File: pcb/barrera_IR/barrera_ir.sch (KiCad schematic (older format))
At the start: 16 parts, among them J1 RJ45, P1 DIN_5, P2 DIN_5, U1 LM358N

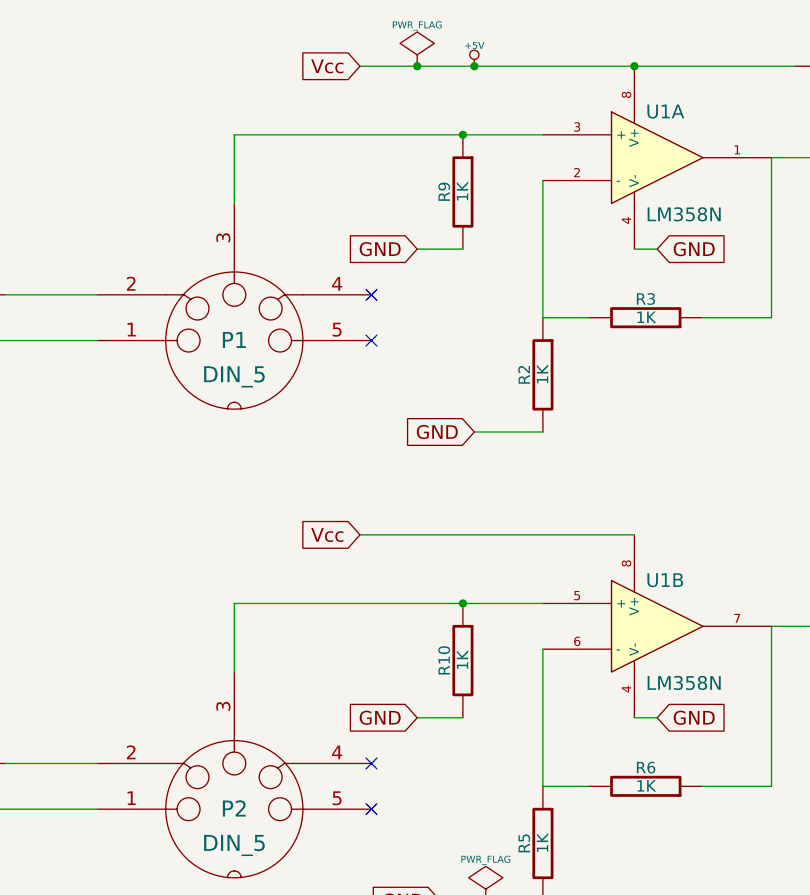
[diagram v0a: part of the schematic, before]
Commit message: correction bug in circuit of infra red barrier
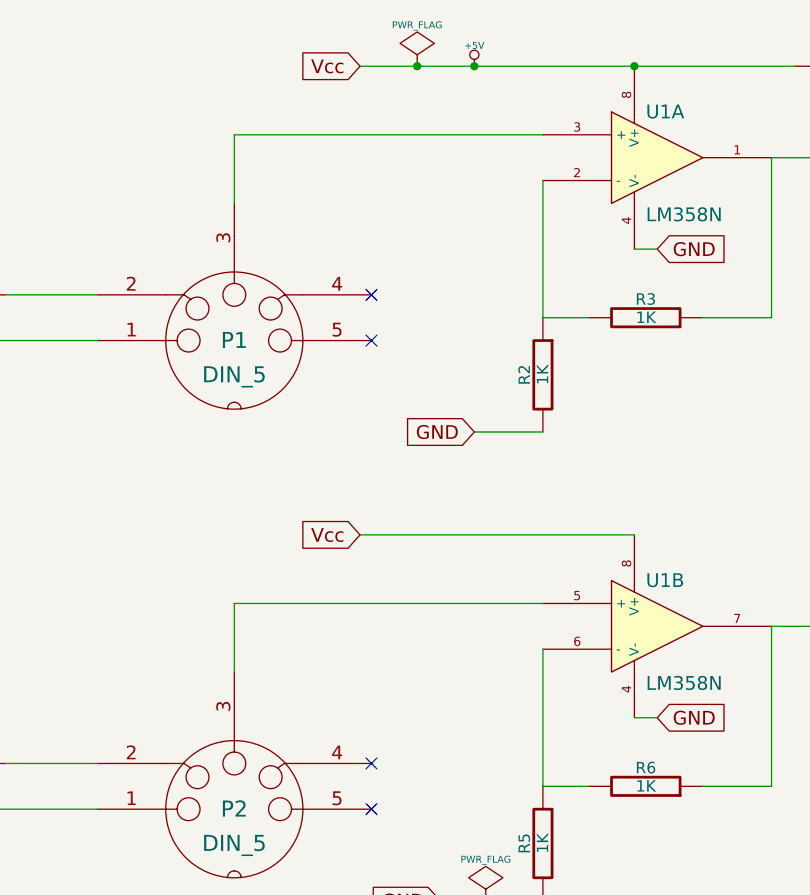
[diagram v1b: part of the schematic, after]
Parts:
- removed R10, R9: 1K, symbol R
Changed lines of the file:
@@
-EESchema Schematic File Version 2  date mar 21 may 2013 21:48:05 UYT
+EESchema Schematic File Version 2  date mié 22 may 2013 19:52:20 UYT
 LIBS:power
 LIBS:device
@@
 LIBS:valves
 LIBS:barrera_ir-cache
-EELAYER 24 0
+EELAYER 27 0
 EELAYER END
 $Descr A4 11693 8268
@@
 F 0 "P1" H 4350 3850 70  0000 C CNN
 F 1 "DIN_5" H 4350 3700 70  0000 C CNN
-F 2 "" H 4350 3850 60  0001 C CNN
-F 3 "" H 4350 3850 60  0001 C CNN
 	1    4350 3850
 	1    0    0    -1
@@
 F 0 "#PWR01" H 5400 2740 20  0001 C CNN
 F 1 "+5V" H 5400 2740 30  0000 C CNN
-F 2 "" H 5400 2650 60  0001 C CNN
-F 3 "" H 5400 2650 60  0001 C CNN
 	1    5400 2650
 	1    0    0    -1
@@
 F 0 "#FLG02" H 5150 2745 30  0001 C CNN
 F 1 "PWR_FLAG" H 5150 2830 30  0000 C CNN
-F 2 "" H 5150 2650 60  0001 C CNN
-F 3 "" H 5150 2650 60  0001 C CNN
 	1    5150 2650
 	1    0    0    -1
@@
 F 0 "R1" V 3180 3650 50  0000 C CNN
 F 1 "390" V 3100 3650 50  0000 C CNN
-F 2 "" H 3100 3650 60  0001 C CNN
-F 3 "" H 3100 3650 60  0001 C CNN
 	1    3100 3650
 	0    1    1    0
@@
 F 0 "R3" V 6230 3750 50  0000 C CNN
 F 1 "1K" V 6150 3750 50  0000 C CNN
-F 2 "" H 6150 3750 60  0001 C CNN
-F 3 "" H 6150 3750 60  0001 C CNN
 	1    6150 3750
 	0    1    -1   0
@@
 F 0 "D1" H 7450 3150 40  0000 C CNN
 F 1 "1N4148" H 7450 2950 40  0000 C CNN
-F 2 "" H 7450 3050 60  0001 C CNN
-F 3 "" H 7450 3050 60  0001 C CNN
 	1    7450 3050
 	-1   0    0    1
@@
 F 0 "U1" H 6150 3250 60  0000 L CNN
 F 1 "LM358N" H 6150 2800 60  0000 L CNN
-F 2 "" H 6200 3050 60  0000 C CNN
-F 3 "" H 6200 3050 60  0000 C CNN
 	1    6200 3050
 	1    0    0    -1
@@
 F 0 "R2" V 5780 4000 50  0000 C CNN
 F 1 "1K" V 5700 4000 50  0000 C CNN
-F 2 "" H 5700 4000 60  0001 C CNN
-F 3 "" H 5700 4000 60  0001 C CNN
 	1    5700 4000
 	-1   0    0    -1
@@
 F 0 "P2" H 4350 5900 70  0000 C CNN
 F 1 "DIN_5" H 4350 5750 70  0000 C CNN
-F 2 "" H 4350 5900 60  0001 C CNN
-F 3 "" H 4350 5900 60  0001 C CNN
 	1    4350 5900
 	1    0    0    -1
@@
 F 0 "R4" V 3180 5700 50  0000 C CNN
 F 1 "390" V 3100 5700 50  0000 C CNN
-F 2 "" H 3100 5700 60  0001 C CNN
-F 3 "" H 3100 5700 60  0001 C CNN
 	1    3100 5700
 	0    1    1    0
@@
 F 0 "R6" V 6230 5800 50  0000 C CNN
 F 1 "1K" V 6150 5800 50  0000 C CNN
-F 2 "" H 6150 5800 60  0001 C CNN
-F 3 "" H 6150 5800 60  0001 C CNN
 	1    6150 5800
 	0    1    -1   0
@@
 F 0 "D2" H 7450 5200 40  0000 C CNN
 F 1 "1N4148" H 7450 5000 40  0000 C CNN
-F 2 "" H 7450 5100 60  0001 C CNN
-F 3 "" H 7450 5100 60  0001 C CNN
 	1    7450 5100
 	-1   0    0    1
@@
 F 0 "U1" H 6150 5300 60  0000 L CNN
 F 1 "LM358N" H 6150 4850 60  0000 L CNN
-F 2 "" H 6200 5100 60  0000 C CNN
-F 3 "" H 6200 5100 60  0000 C CNN
 	2    6200 5100
 	1    0    0    -1
@@
 F 0 "R5" V 5780 6050 50  0000 C CNN
 F 1 "1K" V 5700 6050 50  0000 C CNN
-F 2 "" H 5700 6050 60  0001 C CNN
-F 3 "" H 5700 6050 60  0001 C CNN
 	1    5700 6050
 	-1   0    0    -1
@@
 F 0 "R7" V 7130 2650 50  0000 C CNN
 F 1 "1K" V 7050 2650 50  0000 C CNN
-F 2 "" H 7050 2650 60  0001 C CNN
-F 3 "" H 7050 2650 60  0001 C CNN
 	1    7050 2650
 	0    1    -1   0
@@
 F 0 "#PWR03" H 5450 6400 30  0001 C CNN
 F 1 "GND" H 5450 6330 30  0001 C CNN
-F 2 "" H 5450 6400 60  0000 C CNN
-F 3 "" H 5450 6400 60  0000 C CNN
 	1    5450 6400
 	1    0    0    -1
@@
 F 0 "#FLG04" H 5450 6395 30  0001 C CNN
 F 1 "PWR_FLAG" H 5450 6480 30  0000 C CNN
-F 2 "" H 5450 6300 60  0000 C CNN
-F 3 "" H 5450 6300 60  0000 C CNN
 	1    5450 6300
 	1    0    0    -1
@@
 F 0 "R8" V 9380 5700 50  0000 C CNN
 F 1 "4K7" V 9300 5700 50  0000 C CNN
-F 2 "" H 9300 5700 60  0001 C CNN
-F 3 "" H 9300 5700 60  0001 C CNN
 	1    9300 5700
 	0    1    -1   0
@@
 Wire Wire Line
 	9750 5700 9550 5700
-$Comp
-L R R10
-U 1 1 519BF9E2
-P 5350 5250
-F 0 "R10" V 5430 5250 50  0000 C CNN
-F 1 "1K" V 5350 5250 50  0000 C CNN
-F 2 "" H 5350 5250 60  0001 C CNN
-F 3 "" H 5350 5250 60  0001 C CNN
-	1    5350 5250
-	-1   0    0    -1
-$EndComp
-Text GLabel 5150 5500 0    60   Input ~ 0
-GND
 Wire Wire Line
 	4350 5300 4350 5000
 Wire Wire Line
 	4350 5000 5700 5000
-Connection ~ 5350 5000
-Wire Wire Line
-	5350 5500 5150 5500
-$Comp
-L R R9
-U 1 1 519BFB8A
-P 5350 3200
-F 0 "R9" V 5430 3200 50  0000 C CNN
-F 1 "1K" V 5350 3200 50  0000 C CNN
-F 2 "" H 5350 3200 60  0001 C CNN
-F 3 "" H 5350 3200 60  0001 C CNN
-	1    5350 3200
-	-1   0    0    -1
-$EndComp
-Text GLabel 5150 3450 0    60   Input ~ 0
-GND
 Wire Wire Line
 	4350 2950 5700 2950
-Connection ~ 5350 2950
-Wire Wire Line
-	5350 3450 5150 3450
 Wire Wire Line
 	4350 2950 4350 3250

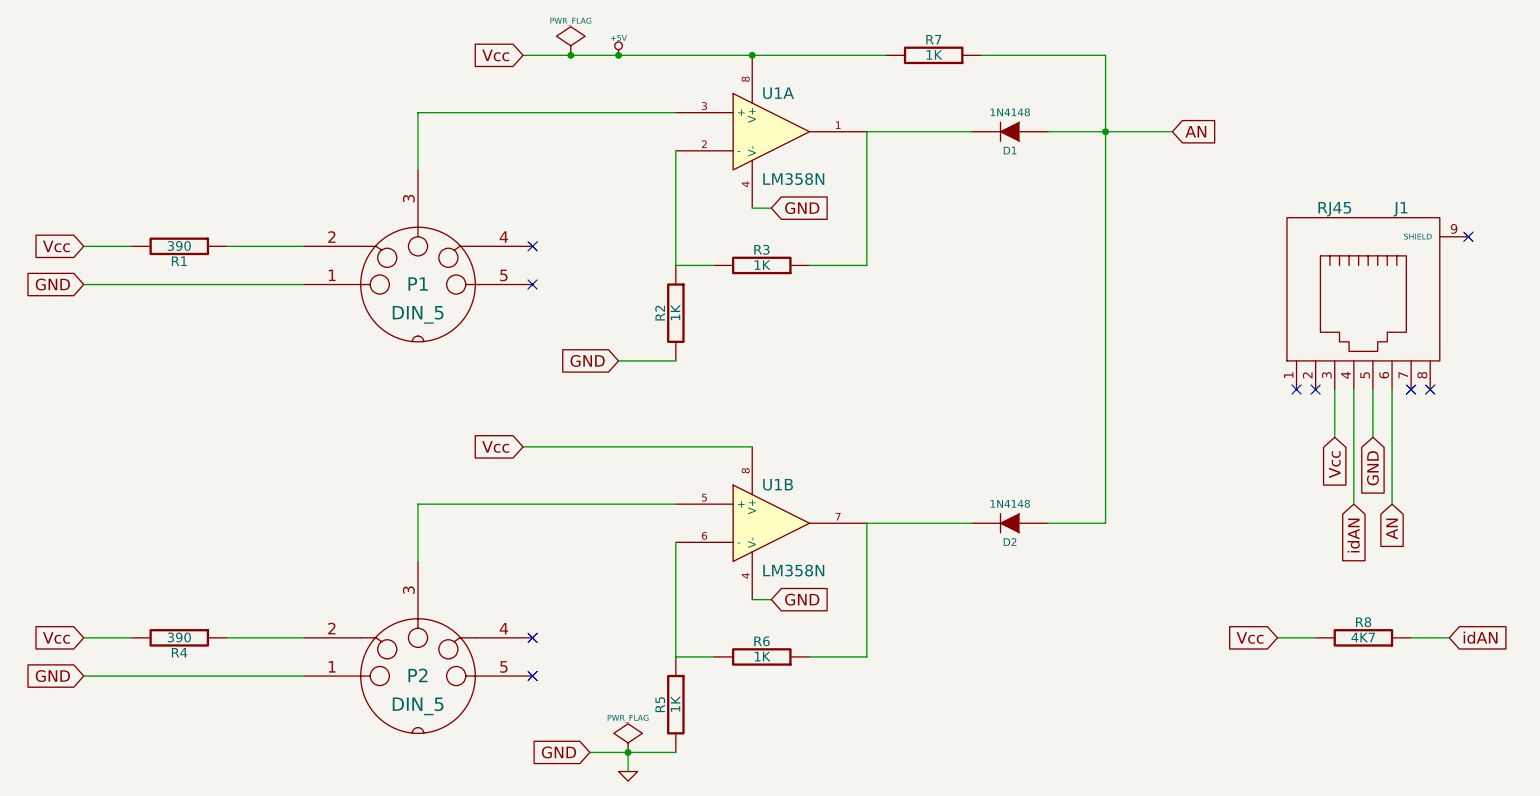
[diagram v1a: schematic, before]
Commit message: Change the wired AND for wired OR in the output of barrier IR
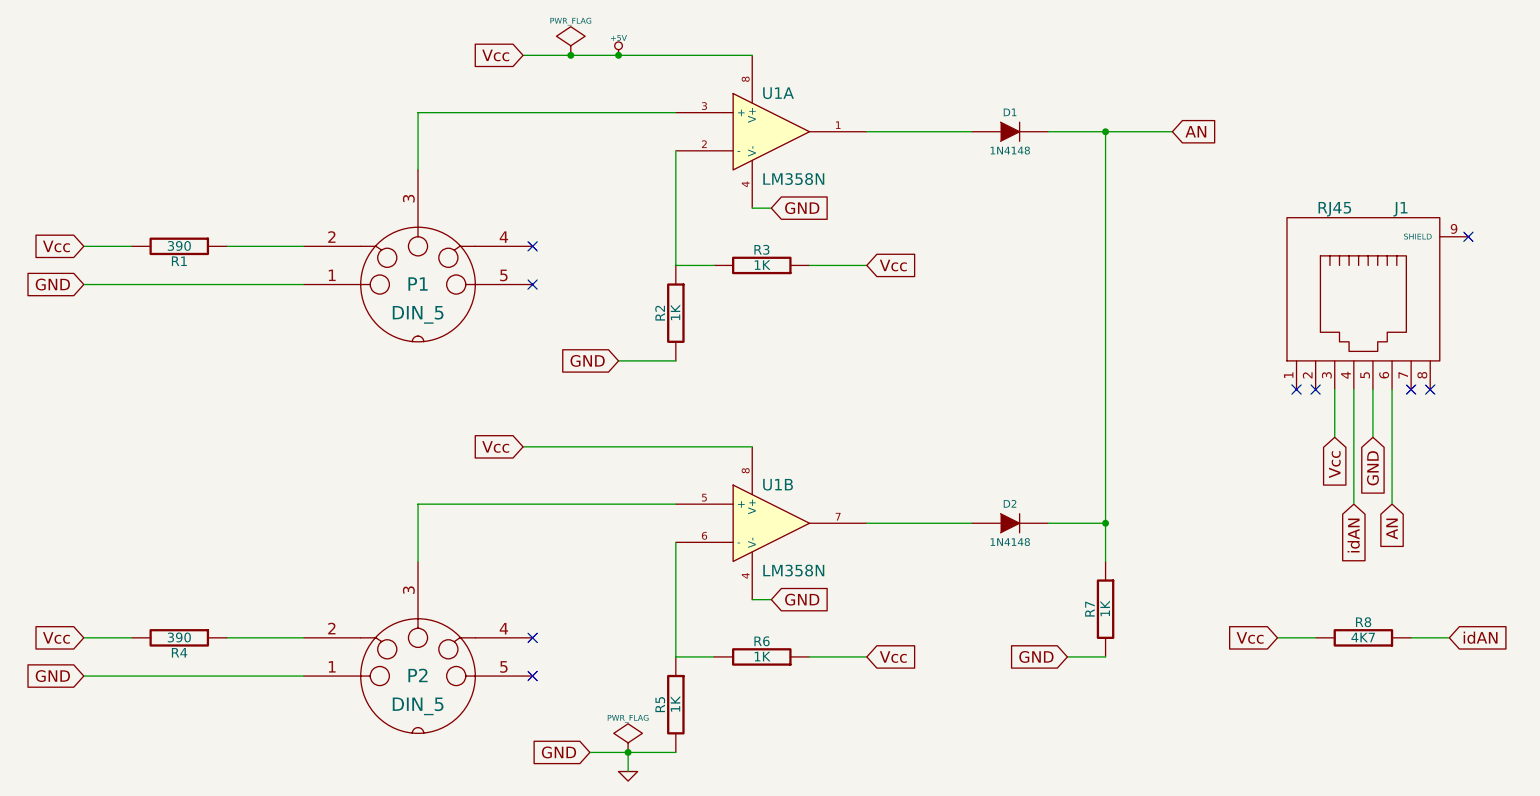
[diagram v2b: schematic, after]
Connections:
- net +5V: now also R3.1, R6.1; no longer R7.2
- net AN: now also D1.2 (K), D2.2 (K); no longer D1.1 (A), D2.1 (A)
- net GND: now also R7.2
- new net: D1.1 (A), U1.1
- new net: D2.1 (A), U1.7
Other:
- moved on the sheet: R7
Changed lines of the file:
@@
-EESchema Schematic File Version 2  date mié 22 may 2013 19:52:20 UYT
+EESchema Schematic File Version 2  date mar 25 jun 2013 20:22:33 UYT
 LIBS:power
 LIBS:device
@@
 Sheet 1 1
 Title "Barrera infrarojo para detectar movimiento"
-Date "22 may 2013"
-Rev "1"
+Date "25 jun 2013"
+Rev "1.2"
 Comp ""
 Comment1 ""
@@
 F 1 "1N4148" H 7450 2950 40  0000 C CNN
 	1    7450 3050
-	-1   0    0    1
+	1    0    0    -1
 $EndComp
 $Comp
@@
 F 1 "1N4148" H 7450 5000 40  0000 C CNN
 	1    7450 5100
-	-1   0    0    1
+	1    0    0    -1
 $EndComp
 $Comp
@@
 L R R7
 U 1 1 51957F9B
-P 7050 2650
-F 0 "R7" V 7130 2650 50  0000 C CNN
-F 1 "1K" V 7050 2650 50  0000 C CNN
-	1    7050 2650
-	0    1    -1   0
+P 7950 5550
+F 0 "R7" V 8030 5550 50  0000 C CNN
+F 1 "1K" V 7950 5550 50  0000 C CNN
+	1    7950 5550
+	-1   0    0    -1
 $EndComp
 $Comp
@@
 Text GLabel 9450 5000 3    60   Input ~ 0
 AN
-Wire Wire Line
-	4900 2650 6800 2650
 Connection ~ 5150 2650
 Wire Wire Line
@@
 	6400 3750 6700 3750
 Wire Wire Line
-	6700 3750 6700 3050
-Wire Wire Line
 	5400 4250 5700 4250
 Wire Wire Line
@@
 	6400 5800 6700 5800
 Wire Wire Line
-	6700 5800 6700 5100
-Wire Wire Line
 	6100 5500 6200 5500
 Wire Wire Line
 	6700 5100 7250 5100
-Connection ~ 6100 2650
-Wire Wire Line
-	7300 2650 7950 2650
-Wire Wire Line
-	7950 2650 7950 5100
+Wire Wire Line
+	7950 3050 7950 5300
 Connection ~ 7950 3050
 Wire Wire Line
@@
 Wire Wire Line
 	4350 2950 4350 3250
+Wire Wire Line
+	4900 2650 6100 2650
+Connection ~ 7950 5100
+Text GLabel 7750 5800 0    60   Input ~ 0
+GND
+Wire Wire Line
+	7750 5800 7950 5800
+Text GLabel 6700 3750 2    60   Input ~ 0
+Vcc
+Text GLabel 6700 5800 2    60   Input ~ 0
+Vcc
 $EndSCHEMATC
